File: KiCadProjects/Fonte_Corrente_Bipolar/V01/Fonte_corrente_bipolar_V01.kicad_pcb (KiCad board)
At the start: 2 copper layers, 90 x 100 mm, 48 parts, among them J1 alimentacao analogica, J2 sinais analogicos, J3 comunicacao / sinais digitais, J4 signal select 1, J5 signal select 2, J7 Vref, U1 INA128, U1-howland1 AD828AN, U2 INA128, U3-cond1 AD828AN

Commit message: Baseado barramento v04 - Finalizado
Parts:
- J4: value signal select 1 -> SinA | Sin1
- J5: value signal select 2 -> SinB | Sin2
- J7: value Vref -> +3.3V | +5.0V
- moved R21 456.9 mm to (165.1, 41.8), turned to 180 degrees
- moved L4:+3.3v1 454.2 mm to (177.0, 44.2)
- moved R22 451.4 mm to (159.8, 47.7), turned to 180 degrees
- moved L3:+5v1 446.8 mm to (170.0, 44.2)
- moved R20 426.3 mm to (134.8, 42.0), turned to 180 degrees
- moved C1 422.0 mm to (147.5, 93.8)
- moved C2 410.8 mm to (136.3, 104.4)
- moved Rganho-I2 403.2 mm to (117.4, 117.0)
- moved Rsentinela-I2 398.7 mm to (112.9, 131.6), turned to 90 degrees
- moved U2-INA-I2 392.6 mm to (117.4, 123.4)
- moved R6 360.8 mm to (119.5, 57.8)
- moved R12 351.2 mm to (177.3, 57.8), turned to -90 degrees
- moved R4 346.9 mm to (125.3, 71.2)
- moved J7 344.1 mm to (160.7, 99.9)
- moved C4 341.7 mm to (170.3, 131.2), turned to 180 degrees
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- renumbered D5 to L1:+9v1, D6 to L2:-9v1, D7 to L3:+5v1, D8 to L4:+3.3v1, RganhoINA1 to Rganho-I1, RganhoINA2 to Rganho-I2, Rsentinela1 to Rsentinela-I1, Rsentinela2 to Rsentinela-I2, U2 to U1-INA-I1, U1 to U2-INA-I2
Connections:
- C1 pad 1: nó3 -> nó4
- C1 pad 2: nó4 -> nó3
- C3 pad 1: nó1 -> nó2
- C3 pad 2: nó2 -> nó1
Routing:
- net -9V: track 0.00 -> 205.6 mm
- net +9V: track 0.00 -> 185.0 mm
- net SinB: track 0.00 -> 145.9 mm, vias 0 -> 1
- net Sin2: track 0.00 -> 141.0 mm, vias 0 -> 1
- net out_corrente_2: track 0.00 -> 122.3 mm
- net Ampl2: track 0.00 -> 99.3 mm
- net SinA: track 0.00 -> 88.8 mm, vias 0 -> 1
- net Sin1: track 0.00 -> 86.2 mm, vias 0 -> 2
- net +5V: track 0.00 -> 81.4 mm
- net +3.3V: track 0.00 -> 81.4 mm
- net Vref: track 0.00 -> 67.1 mm
- net Ampl1: track 0.00 -> 51.9 mm
- net out_corrente_1: track 0.00 -> 43.9 mm
- net V_INA_2: track 0.00 -> 38.4 mm
- net V_INA_1: track 0.00 -> 36.4 mm
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
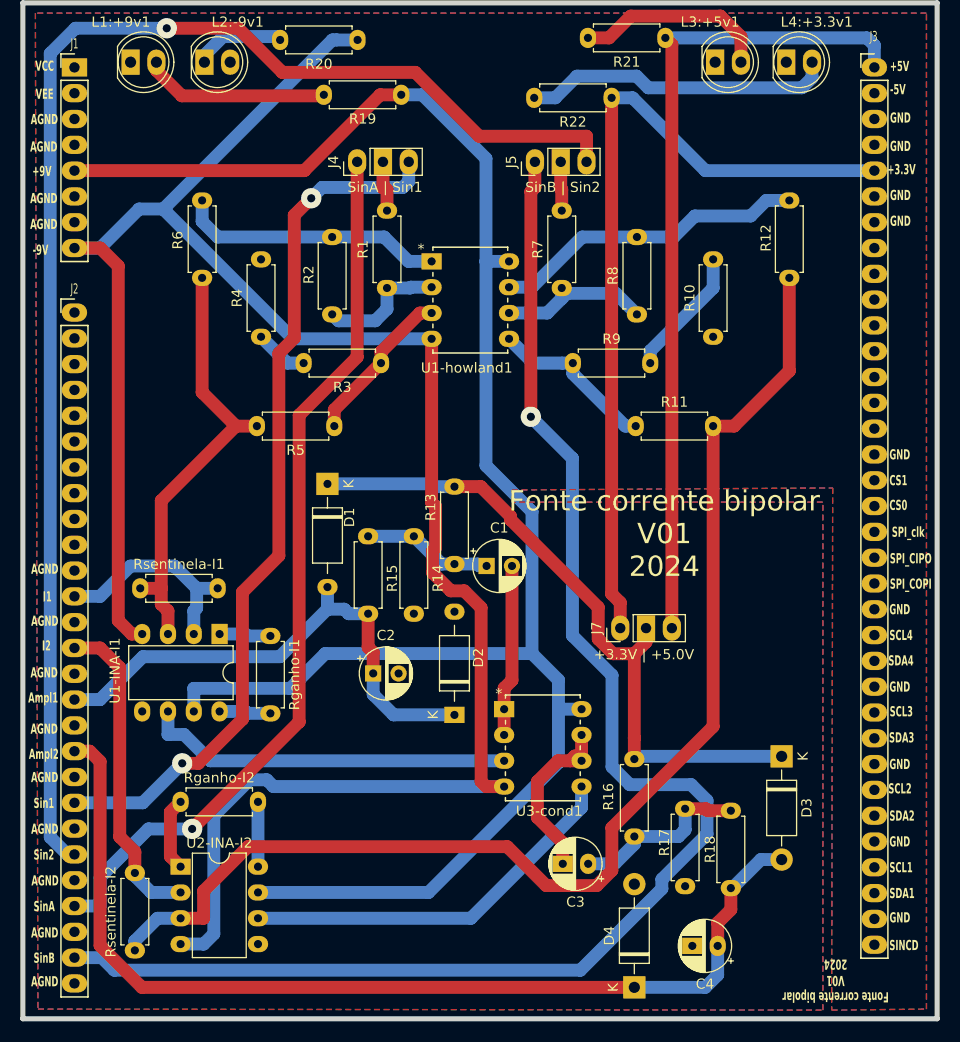
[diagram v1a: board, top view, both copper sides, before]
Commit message: Baseado barramento v04 - Finalizado - implementacao resistor pullup i2c 2
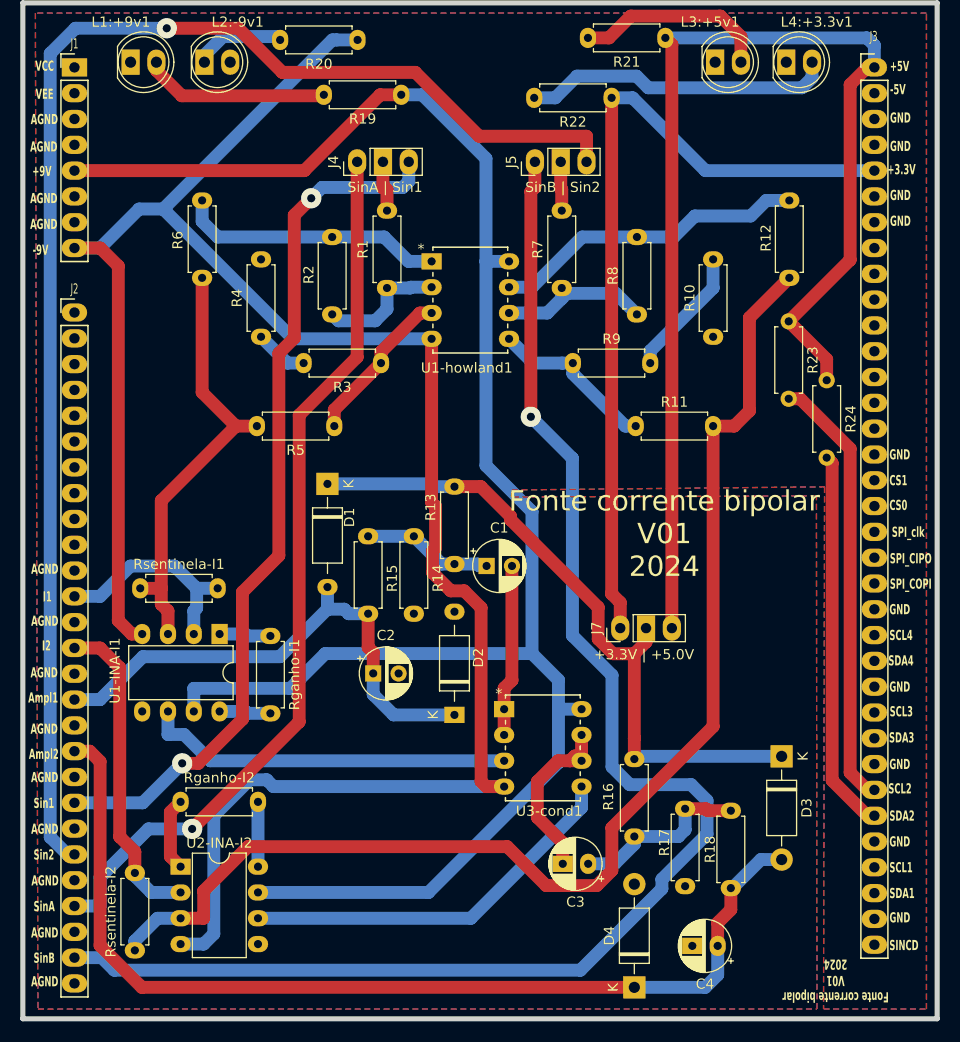
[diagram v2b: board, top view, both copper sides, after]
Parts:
- added R23: 4k7, Resistor_THT:R_Axial_DIN0207_L6.3mm_D2.5mm_P7.62mm_Horizontal, F.Cu at (177.2, 69.7)
- added R24: 4k7, Resistor_THT:R_Axial_DIN0207_L6.3mm_D2.5mm_P7.62mm_Horizontal, F.Cu at (181.0, 75.5)
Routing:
- net SCL2: track 0.00 -> 43.1 mm
- net SDA2: track 0.00 -> 37.6 mm
- net +5V: track 81.4 -> 117.7 mm

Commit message: Baseado barramento v04 - Finalizado
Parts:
- renumbered L4:+3.3v1 to L+3.3v1, L3:+5v1 to L+5v1, L1:+9v1 to L+9v1, L2:-9v1 to L-9v1, R23 to RpSCL2, R24 to RpSDA2
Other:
- board text added: "adc_uC"
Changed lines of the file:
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@@
   (net 70 "V_INA_1")
   (net 71 "Net-(R10-Pad1)")
-  (net 72 "Net-(L1:+9v1-A)")
-  (net 73 "Net-(L2:-9v1-K)")
-  (net 74 "Net-(L3:+5v1-A)")
-  (net 75 "Net-(L4:+3.3v1-A)")
+  (net 72 "Net-(L+3.3v1-A)")
+  (net 73 "Net-(L+5v1-A)")
+  (net 74 "Net-(L+9v1-A)")
+  (net 75 "Net-(L-9v1-K)")
   (footprint "Resistor_THT:R_Axial_DIN0207_L6.3mm_D2.5mm_P7.62mm_Horizontal" (layer "F.Cu")
     (at 135.84 90.86 -90)
@@
     (property "ki_keywords" "R res resistor")
     (attr through_hole)
-    (fp_text reference "R24" (at 3.81 -2.37 90) (layer "F.SilkS")
+    (fp_text reference "RpSDA2" (at 3.81 -2.37 90) (layer "F.SilkS")
         (effects (font (size 1 1) (thickness 0.15)))
     )
@@
     (property "ki_keywords" "LED diode")
     (attr through_hole)
-    (fp_text reference "L2:-9v1" (at 3.275 -3.96) (layer "F.SilkS")
+    (fp_text reference "L-9v1" (at 3.275 -3.96) (layer "F.SilkS")
         (effects (font (size 1 1) (thickness 0.15)))
     )
@@
       (stroke (width 0.1) (type solid)) (fill none) (layer "F.Fab"))
     (pad "1" thru_hole rect (at 0 0) (size 1.8 2.5) (drill 1.1) (layers "*.Cu" "*.Mask")
-      (net 73 "Net-(L2:-9v1-K)") (pinfunction "K") (pintype "passive"))
+      (net 75 "Net-(L-9v1-K)") (pinfunction "K") (pintype "passive"))
     (pad "2" thru_hole oval (at 2.54 0) (size 1.8 2.5) (drill 1.1) (layers "*.Cu" "*.Mask")
       (net 31 "Earth") (pinfunction "A") (pintype "passive"))
@@
     (property "ki_keywords" "LED diode")
     (attr through_hole)
-    (fp_text reference "L1:+9v1" (at -0.96 -3.96) (layer "F.SilkS")
+    (fp_text reference "L+9v1" (at -0.96 -3.96) (layer "F.SilkS")
         (effects (font (size 1 1) (thickness 0.15)))
     )
@@
       (net 31 "Earth") (pinfunction "K") (pintype "passive"))
     (pad "2" thru_hole oval (at 2.54 0) (size 1.8 2.5) (drill 1.1) (layers "*.Cu" "*.Mask")
-      (net 72 "Net-(L1:+9v1-A)") (pinfunction "A") (pintype "passive"))
+      (net 74 "Net-(L+9v1-A)") (pinfunction "A") (pintype "passive"))
     (model "${KICAD6_3DMODEL_DIR}/LED_THT.3dshapes/LED_D5.0mm.wrl"
       (offset (xyz 0 0 0))
@@
       (net 5 "+5V") (pintype "passive"))
     (pad "2" thru_hole oval (at 7.62 0 180) (size 1.6 2) (drill 0.8) (layers "*.Cu" "*.Mask")
-      (net 74 "Net-(L3:+5v1-A)") (pintype "passive"))
+      (net 73 "Net-(L+5v1-A)") (pintype "passive"))
     (model "${KICAD6_3DMODEL_DIR}/Resistor_THT.3dshapes/R_Axial_DIN0207_L6.3mm_D2.5mm_P7.62mm_Horizontal.wrl"
       (offset (xyz 0 0 0))
@@
       (net 7 "+3.3V") (pintype "passive"))
     (pad "2" thru_hole oval (at 7.62 0 180) (size 1.6 2) (drill 0.8) (layers "*.Cu" "*.Mask")
-      (net 75 "Net-(L4:+3.3v1-A)") (pintype "passive"))
+      (net 72 "Net-(L+3.3v1-A)") (pintype "passive"))
     (model "${KICAD6_3DMODEL_DIR}/Resistor_THT.3dshapes/R_Axial_DIN0207_L6.3mm_D2.5mm_P7.62mm_Horizontal.wrl"
       (offset (xyz 0 0 0))
@@
     (property "ki_keywords" "LED diode")
     (attr through_hole)
-    (fp_text reference "L3:+5v1" (at -0.5 -3.96) (layer "F.SilkS")
+    (fp_text reference "L+5v1" (at -0.5 -3.96) (layer "F.SilkS")
         (effects (font (size 1 1) (thickness 0.15)))
     )
@@
       (net 31 "Earth") (pinfunction "K") (pintype "passive"))
     (pad "2" thru_hole oval (at 2.54 0) (size 1.8 2.5) (drill 1.1) (layers "*.Cu" "*.Mask")
-      (net 74 "Net-(L3:+5v1-A)") (pinfunction "A") (pintype "passive"))
+      (net 73 "Net-(L+5v1-A)") (pinfunction "A") (pintype "passive"))
     (model "${KICAD6_3DMODEL_DIR}/LED_THT.3dshapes/LED_D5.0mm.wrl"
       (offset (xyz 0 0 0))
@@
     (property "ki_keywords" "R res resistor")
     (attr through_hole)
-    (fp_text reference "R23" (at 3.81 -2.37 90) (layer "F.SilkS")
+    (fp_text reference "RpSCL2" (at 3.68 2.23 90) (layer "F.SilkS")
         (effects (font (size 1 1) (thickness 0.15)))
     )
@@
     (property "ki_keywords" "LED diode")
     (attr through_hole)
-    (fp_text reference "L4:+3.3v1" (at 3 -3.96) (layer "F.SilkS")
+    (fp_text reference "L+3.3v1" (at 3 -3.96) (layer "F.SilkS")
         (effects (font (size 1 1) (thickness 0.15)))
     )
@@
       (net 31 "Earth") (pinfunction "K") (pintype "passive"))
     (pad "2" thru_hole oval (at 2.54 0) (size 1.8 2.5) (drill 1.1) (layers "*.Cu" "*.Mask")
-      (net 75 "Net-(L4:+3.3v1-A)") (pinfunction "A") (pintype "passive"))
+      (net 72 "Net-(L+3.3v1-A)") (pinfunction "A") (pintype "passive"))
     (model "${KICAD6_3DMODEL_DIR}/LED_THT.3dshapes/LED_D5.0mm.wrl"
       (offset (xyz 0 0 0))
@@
       (net 3 "+9V") (pintype "passive"))
     (pad "2" thru_hole oval (at 7.62 0 180) (size 1.6 2) (drill 0.8) (layers "*.Cu" "*.Mask")
-      (net 72 "Net-(L1:+9v1-A)") (pintype "passive"))
+      (net 74 "Net-(L+9v1-A)") (pintype "passive"))
     (model "${KICAD6_3DMODEL_DIR}/Resistor_THT.3dshapes/R_Axial_DIN0207_L6.3mm_D2.5mm_P7.62mm_Horizontal.wrl"
       (offset (xyz 0 0 0))
@@
       (net 4 "-9V") (pintype "passive"))
     (pad "2" thru_hole oval (at 7.62 0 180) (size 1.6 2) (drill 0.8) (layers "*.Cu" "*.Mask")
-      (net 73 "Net-(L2:-9v1-K)") (pintype "passive"))
+      (net 75 "Net-(L-9v1-K)") (pintype "passive"))
     (model "${KICAD6_3DMODEL_DIR}/Resistor_THT.3dshapes/R_Axial_DIN0207_L6.3mm_D2.5mm_P7.62mm_Horizontal.wrl"
       (offset (xyz 0 0 0))
@@
     (effects (font (size 1 0.6) (thickness 0.15) bold) (justify left bottom))
   )
+  (gr_text "adc_uC\n" (at 167.07 99.9) (layer "F.SilkS")
+    (effects (font (size 1 1) (thickness 0.15)) (justify left bottom))
+  )
   (gr_text "SPI_COPI\n" (at 189.254 95.554) (layer "F.SilkS")
     (effects (font (size 1 0.6) (thickness 0.15) bold))
@@
   (segment (start 169.8 66.42) (end 163.61 72.61) (width 1.27) (layer "B.Cu") (net 71))
   (segment (start 169.8 63.6) (end 169.8 66.42) (width 1.27) (layer "B.Cu") (net 71))
-  (segment (start 117.5 47.5) (end 131.38 47.5) (width 1.27) (layer "F.Cu") (net 72))
-  (segment (start 115 45) (end 117.5 47.5) (width 1.27) (layer "F.Cu") (net 72))
-  (segment (start 115 44.19) (end 115 45) (width 1.27) (layer "F.Cu") (net 72))
-  (segment (start 131.38 47.5) (end 131.48 47.4) (width 1.27) (layer "F.Cu") (net 72))
-  (segment (start 119.725 44.19) (end 119.725 43.502075) (width 1.27) (layer "B.Cu") (net 73))
-  (segment (start 121.557075 41.67) (end 126.85 41.67) (width 1.27) (layer "B.Cu") (net 73))
-  (segment (start 119.725 43.502075) (end 121.557075 41.67) (width 1.27) (layer "B.Cu") (net 73))
-  (segment (start 126.85 41.67) (end 127.18 42) (width 1.27) (layer "B.Cu") (net 73))
-  (segment (start 172.54 41.67) (end 170.5213 39.6513) (width 1.27) (layer "F.Cu") (net 74))
-  (segment (start 172.54 44.19) (end 172.54 41.67) (width 1.27) (layer "F.Cu") (net 74))
-  (segment (start 157.48 41.8) (end 159.55 41.8) (width 1.27) (layer "F.Cu") (net 74))
-  (segment (start 161.6987 39.6513) (end 159.55 41.8) (width 1.27) (layer "F.Cu") (net 74))
-  (segment (start 170.5213 39.6513) (end 161.6987 39.6513) (width 1.27) (layer "F.Cu") (net 74))
-  (segment (start 178.55 46.71) (end 163.4121 46.71) (width 1.27) (layer "B.Cu") (net 75))
-  (segment (start 162.2646 45.5625) (end 156.3975 45.5625) (width 1.27) (layer "B.Cu") (net 75))
-  (segment (start 163.4121 46.71) (end 162.2646 45.5625) (width 1.27) (layer "B.Cu") (net 75))
-  (segment (start 179.54 45.72) (end 178.55 46.71) (width 1.27) (layer "B.Cu") (net 75))
-  (segment (start 179.54 44.19) (end 179.54 45.72) (width 1.27) (layer "B.Cu") (net 75))
-  (segment (start 154.26 47.7) (end 152.19 47.7) (width 1.27) (layer "B.Cu") (net 75))
-  (segment (start 156.3975 45.5625) (end 154.26 47.7) (width 1.27) (layer "B.Cu") (net 75))
+  (segment (start 178.55 46.71) (end 163.4121 46.71) (width 1.27) (layer "B.Cu") (net 72))
+  (segment (start 162.2646 45.5625) (end 156.3975 45.5625) (width 1.27) (layer "B.Cu") (net 72))
+  (segment (start 163.4121 46.71) (end 162.2646 45.5625) (width 1.27) (layer "B.Cu") (net 72))
+  (segment (start 179.54 45.72) (end 178.55 46.71) (width 1.27) (layer "B.Cu") (net 72))
+  (segment (start 179.54 44.19) (end 179.54 45.72) (width 1.27) (layer "B.Cu") (net 72))
+  (segment (start 154.26 47.7) (end 152.19 47.7) (width 1.27) (layer "B.Cu") (net 72))
+  (segment (start 156.3975 45.5625) (end 154.26 47.7) (width 1.27) (layer "B.Cu") (net 72))
+  (segment (start 172.54 41.67) (end 170.5213 39.6513) (width 1.27) (layer "F.Cu") (net 73))
+  (segment (start 172.54 44.19) (end 172.54 41.67) (width 1.27) (layer "F.Cu") (net 73))
+  (segment (start 157.48 41.8) (end 159.55 41.8) (width 1.27) (layer "F.Cu") (net 73))
+  (segment (start 161.6987 39.6513) (end 159.55 41.8) (width 1.27) (layer "F.Cu") (net 73))
+  (segment (start 170.5213 39.6513) (end 161.6987 39.6513) (width 1.27) (layer "F.Cu") (net 73))
+  (segment (start 117.5 47.5) (end 131.38 47.5) (width 1.27) (layer "F.Cu") (net 74))
+  (segment (start 115 45) (end 117.5 47.5) (width 1.27) (layer "F.Cu") (net 74))
+  (segment (start 115 44.19) (end 115 45) (width 1.27) (layer "F.Cu") (net 74))
+  (segment (start 131.38 47.5) (end 131.48 47.4) (width 1.27) (layer "F.Cu") (net 74))
+  (segment (start 119.725 44.19) (end 119.725 43.502075) (width 1.27) (layer "B.Cu") (net 75))
+  (segment (start 121.557075 41.67) (end 126.85 41.67) (width 1.27) (layer "B.Cu") (net 75))
+  (segment (start 119.725 43.502075) (end 121.557075 41.67) (width 1.27) (layer "B.Cu") (net 75))
+  (segment (start 126.85 41.67) (end 127.18 42) (width 1.27) (layer "B.Cu") (net 75))
   (zone (net 31) (net_name "Earth") (layers "F&B.Cu") (hatch edge 0.5)
     (connect_pads yes (clearance 0.5))

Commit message: temp
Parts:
- added RpSCL1: 4k7, Resistor_THT:R_Axial_DIN0207_L6.3mm_D2.5mm_P7.62mm_Horizontal, F.Cu at (179.0, 68.0)
- added RpSCL3: 4k7, Resistor_THT:R_Axial_DIN0207_L6.3mm_D2.5mm_P7.62mm_Horizontal, F.Cu at (158.0, 79.4)
- added RpSCL4: 4k7, Resistor_THT:R_Axial_DIN0207_L6.3mm_D2.5mm_P7.62mm_Horizontal, F.Cu at (163.0, 79.4)
- added RpSDA1: 4k7, Resistor_THT:R_Axial_DIN0207_L6.3mm_D2.5mm_P7.62mm_Horizontal, F.Cu at (179.0, 58.0)
- added RpSDA3: 4k7, Resistor_THT:R_Axial_DIN0207_L6.3mm_D2.5mm_P7.62mm_Horizontal, F.Cu at (168.0, 79.4)
- added RpSDA4: 4k7, Resistor_THT:R_Axial_DIN0207_L6.3mm_D2.5mm_P7.62mm_Horizontal, F.Cu at (173.0, 79.4)
- moved RpSDA2 22.6 mm to (179.0, 53.0), turned to 180 degrees
- moved R12 13.1 mm to (166.0, 51.2)
- moved R11 7.82 mm to (168.2, 75.0)
- moved RpSCL2 6.93 mm to (179.0, 63.0), turned to 180 degrees
- moved R10 2.80 mm to (167.0, 63.6)
- moved R8 1.32 mm to (161.0, 68.8)
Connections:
- RpSCL2 pad 1: +5V -> SCL3
- RpSCL2 pad 2: SCL2 -> +3.3V
- RpSDA2 pad 1: +5V -> SDA3
- RpSDA2 pad 2: SDA2 -> +3.3V
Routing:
- net SDA3: track 0.00 -> 87.4 mm
- net SCL1: track 0.00 -> 86.1 mm
- net SDA1: track 0.00 -> 72.2 mm, vias 0 -> 1
- net SCL3: track 0.00 -> 48.9 mm
- net SinA: track 88.8 -> 133.4 mm
- net SCL4: track 0.00 -> 28.3 mm
- net SDA4: track 0.00 -> 25.4 mm, vias 0 -> 1
- net +5V: track 117.7 -> 94.1 mm
- net -9V: track 205.6 -> 189.3 mm
- net SinB: track 145.9 -> 130.0 mm, vias 1 -> 0
- net Ampl2: track 99.3 -> 109.2 mm
- net SDA2: track 37.6 -> 43.4 mm, vias 0 -> 1
- net Net-(U1-howland1-OUT2): track 31.1 -> 25.5 mm
- net Net-(U1-howland1-+IN2): track 16.6 -> 21.8 mm
- net +9V: track 185.0 -> 190.1 mm
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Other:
- board text added: "Signal - I1"
- board text added: "Signal - I2"
